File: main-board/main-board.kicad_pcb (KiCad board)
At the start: 2 copper layers, 210 x 130 mm, 173 parts, among them J1 PWR_SELECT, J10 Conn_02x05_Odd_Even, J11 Conn_02x05_Odd_Even, J12 Conn_02x05_Odd_Even, J13 Conn_02x05_Odd_Even, J14 Conn_02x05_Odd_Even, J15 Conn_02x05_Odd_Even, J16 COMM_3, J17 Modular board connector, J18 PWR_EXT_1, J19 PWR_EXT_2, J2 COMM1, J20 COMM_4, J21 COMM_OUT, J3 ICSP, J4 Conn_02x03_Top_Bottom, J5 COMM_2, J7 Conn_02x05_Odd_Even, J8 Conn_02x05_Odd_Even, J9 Conn_02x05_Odd_Even, SW1 RESET, SW10 SW_Push, SW11 SW_Push, SW12 SW_SP3T_x08, SW13 SW_Push, SW14 SW_Push, SW15 SW_Push, SW16 SW_Push, SW17 SW_Push, SW18 SW_Push, SW19 SW_Push, SW2 BTN_LEVEL, SW20 SW_Push, SW21 SW_SP3T_x08, SW22 SW_Push, SW23 SW_Push, SW24 SW_Push, SW25 SW_Push, SW26 SW_Push, SW27 SW_Push, SW28 SW_Push, SW29 SW_Push, SW3 LED_GND, SW30 SW_SP3T_x08, SW31 SW_Push, SW32 SW_Push, SW33 SW_Push, SW34 SW_Push, SW35 SW_Push, SW36 SW_Push, SW37 SW_Push, SW38 SW_Push, SW39 SW_SP3T_x08, SW4 SW_Push, SW41 PWR_EN, SW5 SW_Push, SW6 SW_Push, SW7 SW_Push, SW8 SW_Push, SW9 SW_Push, U1 LM2576HVS-5, U2 AP1117-33, U3 AP1117-18, U4 FT232RL

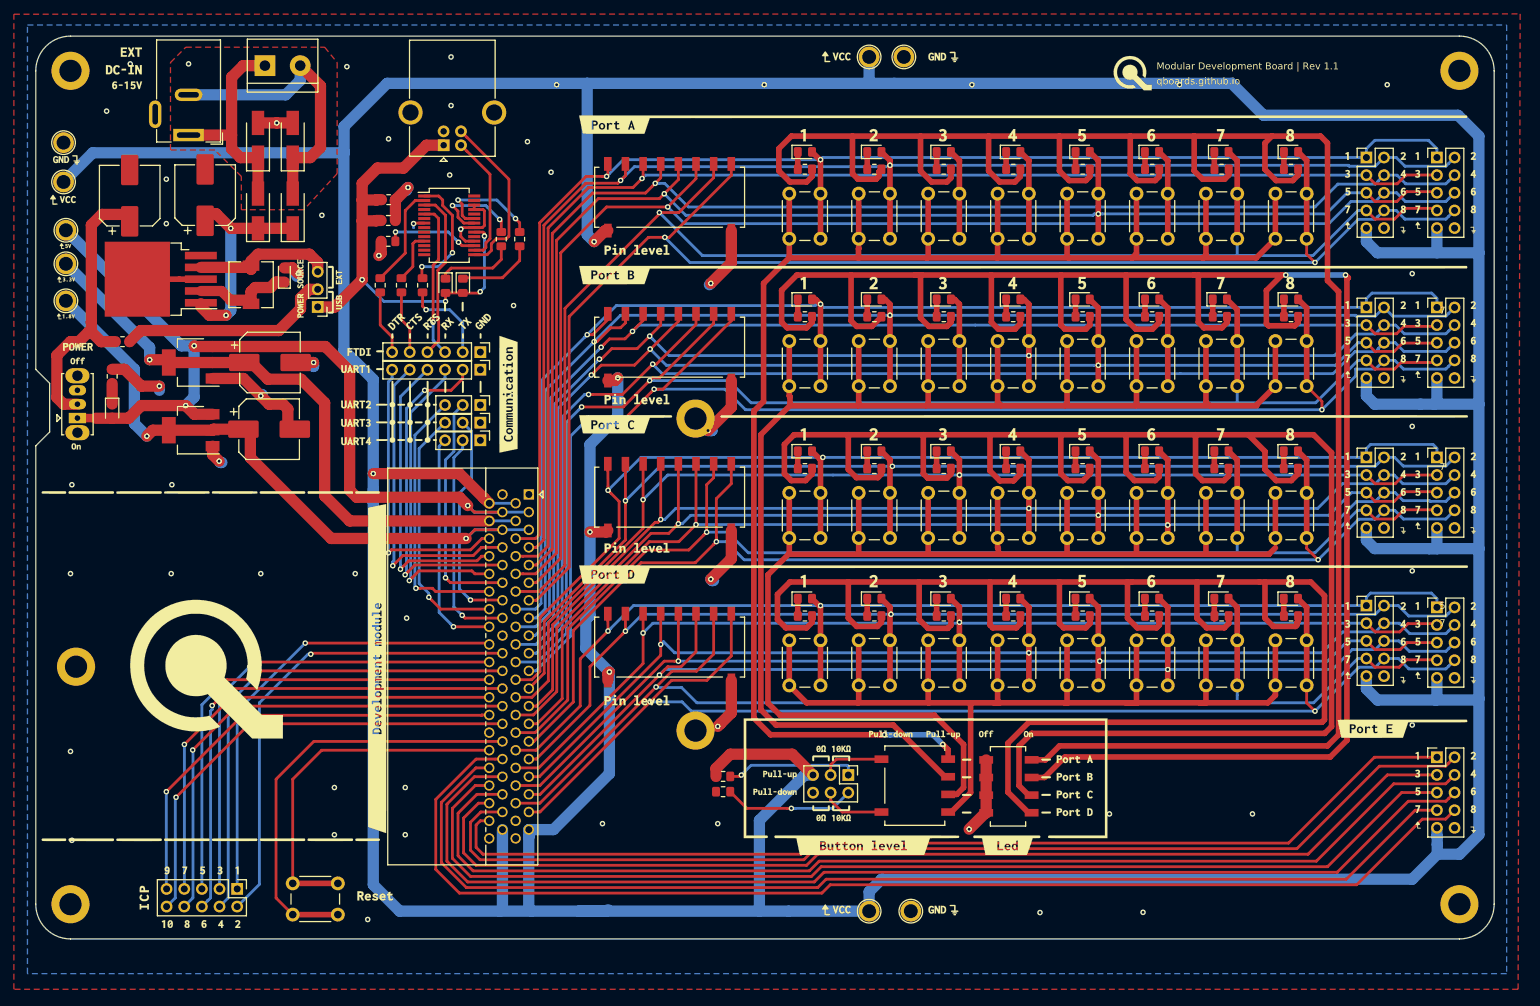
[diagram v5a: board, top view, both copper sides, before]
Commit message: Added pin pullups/downs instead of button level
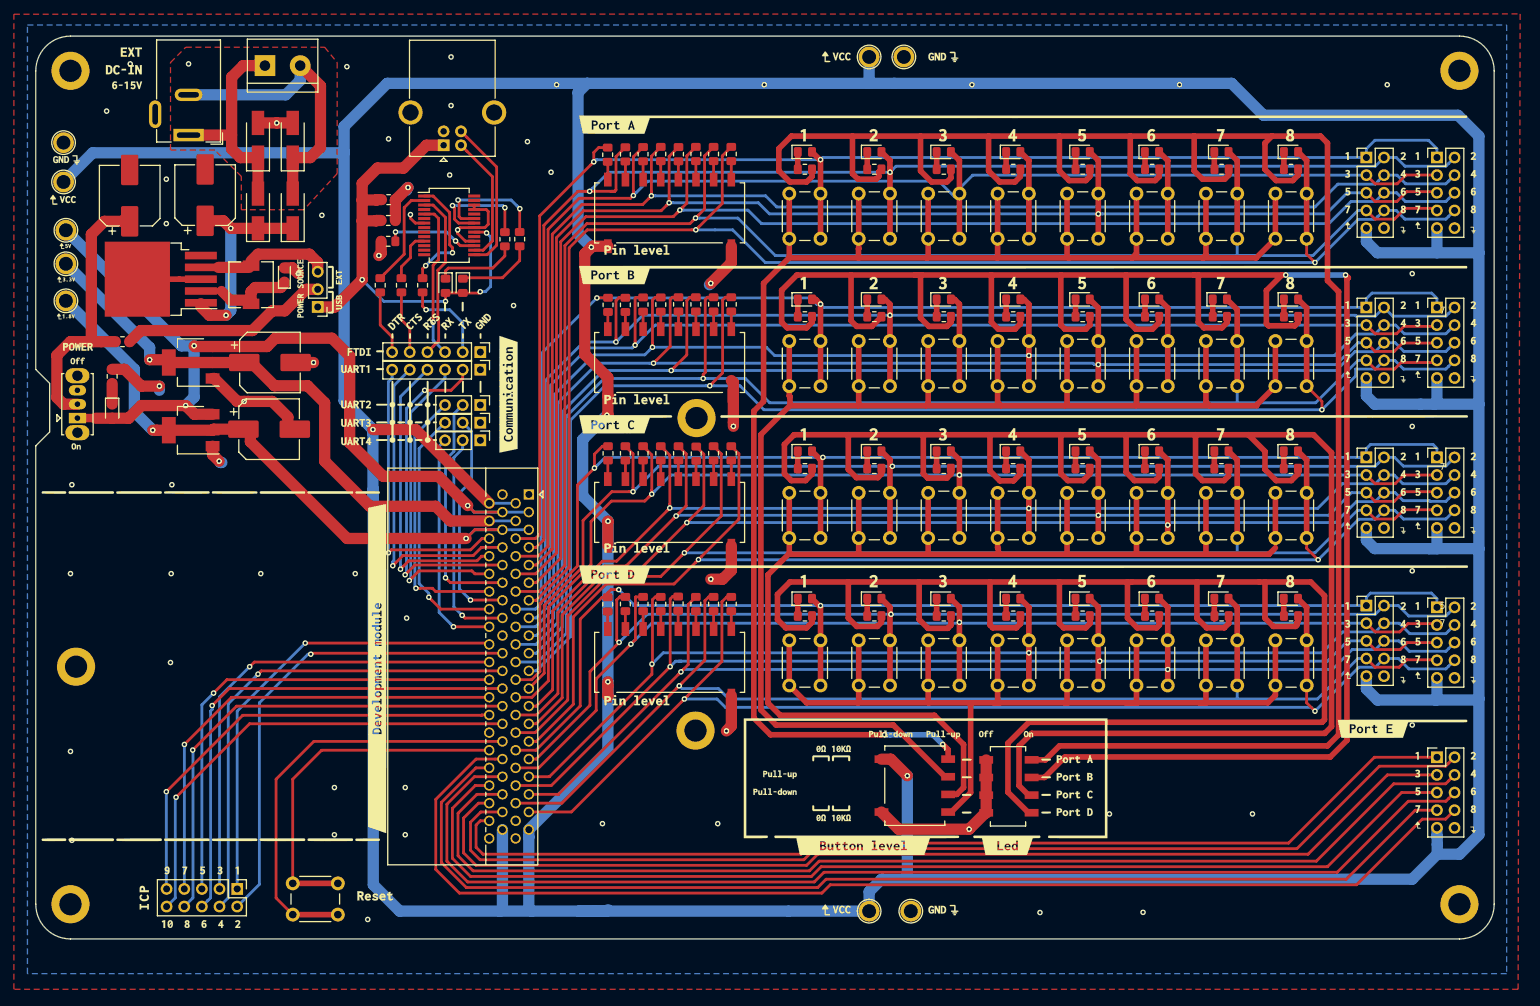
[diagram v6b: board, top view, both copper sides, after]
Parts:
- removed J4: Conn_02x03_Top_Bottom, Connector_PinHeader_2.54mm:PinHeader_2x03_P2.54mm_Vertical
- removed Modular Development Board | Rev 1.1: LOGO_BRD_REF, qboards_aesthetics:logo_url-5mm
- removed R8, R9: R_Small, Resistor_SMD:R_0805_2012Metric_Pad1.15x1.40mm_HandSolder
- removed [BRD_REF]: LOGO_BRD_REF, qboards_aesthetics:logo-20mm
- added R1: 4K7, Resistor_SMD:R_0805_2012Metric_Pad1.15x1.40mm_HandSolder, F.Cu at (119.3, 35.1)
- added R42: 4K7, Resistor_SMD:R_0805_2012Metric_Pad1.15x1.40mm_HandSolder, F.Cu at (121.9, 35.0)
- added R43: 4K7, Resistor_SMD:R_0805_2012Metric_Pad1.15x1.40mm_HandSolder, F.Cu at (124.5, 35.0)
- added R44: 4K7, Resistor_SMD:R_0805_2012Metric_Pad1.15x1.40mm_HandSolder, F.Cu at (127.0, 35.0)
- added R45: 4K7, Resistor_SMD:R_0805_2012Metric_Pad1.15x1.40mm_HandSolder, F.Cu at (129.6, 35.0)
- added R46: 4K7, Resistor_SMD:R_0805_2012Metric_Pad1.15x1.40mm_HandSolder, F.Cu at (132.1, 35.0)
- added R47: 4K7, Resistor_SMD:R_0805_2012Metric_Pad1.15x1.40mm_HandSolder, F.Cu at (134.6, 35.0)
- added R48: 4K7, Resistor_SMD:R_0805_2012Metric_Pad1.15x1.40mm_HandSolder, F.Cu at (137.2, 35.0)
- added R49: 4K7, Resistor_SMD:R_0805_2012Metric_Pad1.15x1.40mm_HandSolder, F.Cu at (119.4, 56.7)
- added R50: 4K7, Resistor_SMD:R_0805_2012Metric_Pad1.15x1.40mm_HandSolder, F.Cu at (121.9, 56.7)
- added R51: 4K7, Resistor_SMD:R_0805_2012Metric_Pad1.15x1.40mm_HandSolder, F.Cu at (124.5, 56.6)
- added R52: 4K7, Resistor_SMD:R_0805_2012Metric_Pad1.15x1.40mm_HandSolder, F.Cu at (127.0, 56.6)
- added R53: 4K7, Resistor_SMD:R_0805_2012Metric_Pad1.15x1.40mm_HandSolder, F.Cu at (129.6, 56.6)
- added R54: 4K7, Resistor_SMD:R_0805_2012Metric_Pad1.15x1.40mm_HandSolder, F.Cu at (132.1, 56.6)
- added R55: 4K7, Resistor_SMD:R_0805_2012Metric_Pad1.15x1.40mm_HandSolder, F.Cu at (134.6, 56.6)
- added R56: 4K7, Resistor_SMD:R_0805_2012Metric_Pad1.15x1.40mm_HandSolder, F.Cu at (137.2, 56.6)
- added R57: 4K7, Resistor_SMD:R_0805_2012Metric_Pad1.15x1.40mm_HandSolder, F.Cu at (119.4, 78.1)
- added R58: 4K7, Resistor_SMD:R_0805_2012Metric_Pad1.15x1.40mm_HandSolder, F.Cu at (121.9, 78.1)
- added R59: 4K7, Resistor_SMD:R_0805_2012Metric_Pad1.15x1.40mm_HandSolder, F.Cu at (124.5, 78.1)
- added R60: 4K7, Resistor_SMD:R_0805_2012Metric_Pad1.15x1.40mm_HandSolder, F.Cu at (127.0, 78.1)
- added R61: 4K7, Resistor_SMD:R_0805_2012Metric_Pad1.15x1.40mm_HandSolder, F.Cu at (129.6, 78.1)
- added R62: 4K7, Resistor_SMD:R_0805_2012Metric_Pad1.15x1.40mm_HandSolder, F.Cu at (132.1, 78.1)
- added R63: 4K7, Resistor_SMD:R_0805_2012Metric_Pad1.15x1.40mm_HandSolder, F.Cu at (134.6, 78.1)
- added R64: 4K7, Resistor_SMD:R_0805_2012Metric_Pad1.15x1.40mm_HandSolder, F.Cu at (137.2, 78.1)
- added R65: 4K7, Resistor_SMD:R_0805_2012Metric_Pad1.15x1.40mm_HandSolder, F.Cu at (119.3, 99.8)
- added R66: 4K7, Resistor_SMD:R_0805_2012Metric_Pad1.15x1.40mm_HandSolder, F.Cu at (121.9, 99.8)
- added R67: 4K7, Resistor_SMD:R_0805_2012Metric_Pad1.15x1.40mm_HandSolder, F.Cu at (124.5, 99.8)
- added R68: 4K7, Resistor_SMD:R_0805_2012Metric_Pad1.15x1.40mm_HandSolder, F.Cu at (127.0, 99.8)
- added R69: 4K7, Resistor_SMD:R_0805_2012Metric_Pad1.15x1.40mm_HandSolder, F.Cu at (129.5, 99.7)
- added R70: 4K7, Resistor_SMD:R_0805_2012Metric_Pad1.15x1.40mm_HandSolder, F.Cu at (132.1, 99.8)
- added R71: 4K7, Resistor_SMD:R_0805_2012Metric_Pad1.15x1.40mm_HandSolder, F.Cu at (134.6, 99.8)
- added R72: 4K7, Resistor_SMD:R_0805_2012Metric_Pad1.15x1.40mm_HandSolder, F.Cu at (137.2, 99.8)
- R3, R4, R5: value 10 -> 10K
- TP_GND3: value VBUS -> GND
- TP_VBUS2: value GND -> VBUS
- moved SW12 2.25 mm to (128.3, 43.5)
- moved SW21 2.20 mm to (128.3, 65.0)
- moved SW39 2.20 mm to (128.3, 108.2)
- moved SW30 2.20 mm to (128.3, 86.6)
- moved R7 0.52 mm to (104.5, 47.2)
- moved H5 0.17 mm to (132.2, 73.0)
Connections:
- SW12 pad 1: /PORT_A_PIN1 -> Net-(R1-Pad2)
- SW12 pad 2: /PORT_A_PIN2 -> Net-(R42-Pad2)
- SW12 pad 3: /PORT_A_PIN3 -> Net-(R43-Pad2)
- SW12 pad 4: /PORT_A_PIN4 -> Net-(R44-Pad2)
- SW12 pad 5: /PORT_A_PIN5 -> Net-(R45-Pad2)
- SW12 pad 6: /PORT_A_PIN6 -> Net-(R46-Pad2)
- SW12 pad 7: /PORT_A_PIN7 -> Net-(R47-Pad2)
- SW12 pad 8: /PORT_A_PIN8 -> Net-(R48-Pad2)
- SW2 pad +: Net-(J4-Pad3) -> VBUS
- SW2 pad -: Net-(J4-Pad4) -> GND
- SW21 pad 1: /PORT_B_PIN1 -> Net-(R49-Pad2)
- SW21 pad 2: /PORT_B_PIN2 -> Net-(R50-Pad2)
- SW21 pad 3: /PORT_B_PIN3 -> Net-(R51-Pad2)
- SW21 pad 4: /PORT_B_PIN4 -> Net-(R52-Pad2)
- SW21 pad 5: /PORT_B_PIN5 -> Net-(R53-Pad2)
- SW21 pad 6: /PORT_B_PIN6 -> Net-(R54-Pad2)
- SW21 pad 7: /PORT_B_PIN7 -> Net-(R55-Pad2)
- SW21 pad 8: /PORT_B_PIN8 -> Net-(R56-Pad2)
- SW30 pad 1: /PORT_C_PIN1 -> Net-(R57-Pad2)
- SW30 pad 2: /PORT_C_PIN2 -> Net-(R58-Pad2)
- SW30 pad 3: /PORT_C_PIN3 -> Net-(R59-Pad2)
- SW30 pad 4: /PORT_C_PIN4 -> Net-(R60-Pad2)
- SW30 pad 5: /PORT_C_PIN5 -> Net-(R61-Pad2)
- SW30 pad 6: /PORT_C_PIN6 -> Net-(R62-Pad2)
- SW30 pad 7: /PORT_C_PIN7 -> Net-(R63-Pad2)
- SW30 pad 8: /PORT_C_PIN8 -> Net-(R64-Pad2)
- SW39 pad 1: /PORT_D_PIN1 -> Net-(R65-Pad2)
- SW39 pad 2: /PORT_D_PIN2 -> Net-(R66-Pad2)
- SW39 pad 3: /PORT_D_PIN3 -> Net-(R67-Pad2)
- SW39 pad 4: /PORT_D_PIN4 -> Net-(R68-Pad2)
- SW39 pad 5: /PORT_D_PIN5 -> Net-(R69-Pad2)
- SW39 pad 6: /PORT_D_PIN6 -> Net-(R70-Pad2)
- SW39 pad 7: /PORT_D_PIN7 -> Net-(R71-Pad2)
- SW39 pad 8: /PORT_D_PIN8 -> Net-(R72-Pad2)
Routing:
- net Net-(J4-Pad1): track 19.0 -> 0.00 mm, vias 1 -> 0
- net Net-(J4-Pad2): track 18.9 -> 0.00 mm, vias 1 -> 0
- net Net-(J4-Pad3): track 9.23 -> 0.00 mm
- net Net-(J4-Pad4): track 9.23 -> 0.00 mm
- net /PORT_A_PIN2: track 199.9 -> 208.3 mm
- net /PORT_C_PIN7: track 180.9 -> 187.3 mm
- net /PORT_C_PIN8: track 185.3 -> 191.6 mm
- net /PORT_B_PIN3: track 188.3 -> 194.2 mm, vias 2 -> 1
- net /PORT_A_PIN8: track 213.6 -> 219.4 mm
- net /PORT_D_PIN2: track 162.4 -> 167.9 mm
- net /PORT_D_PIN3: track 160.7 -> 166.2 mm
- net GND: track 115.9 -> 120.9 mm
- net /PORT_D_PIN4: track 163.3 -> 168.1 mm
- net /PORT_C_PIN3: track 175.0 -> 179.8 mm
- net /PORT_C_PIN6: track 175.8 -> 180.5 mm
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
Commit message: Fixed some routing
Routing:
- net Net-(J17-Pad20): track 44.8 -> 42.7 mm
- net GND: track 120.9 -> 119.0 mm
- net /PORT_B_PIN6: track 198.2 -> 196.6 mm, vias 1 -> 2
- net Net-(J17-Pad24): track 39.7 -> 38.1 mm
- net +3V3: track 86.0 -> 87.6 mm
- net +5V: track 127.0 -> 128.5 mm
- net /PORT_C_PIN1: track 180.4 -> 181.6 mm
- net Net-(J17-Pad14): track 46.1 -> 44.9 mm
- net Net-(J16-Pad3): track 36.7 -> 35.5 mm
- net +1V8: track 91.9 -> 91.1 mm
- net VBUS: track 893.7 -> 893.0 mm

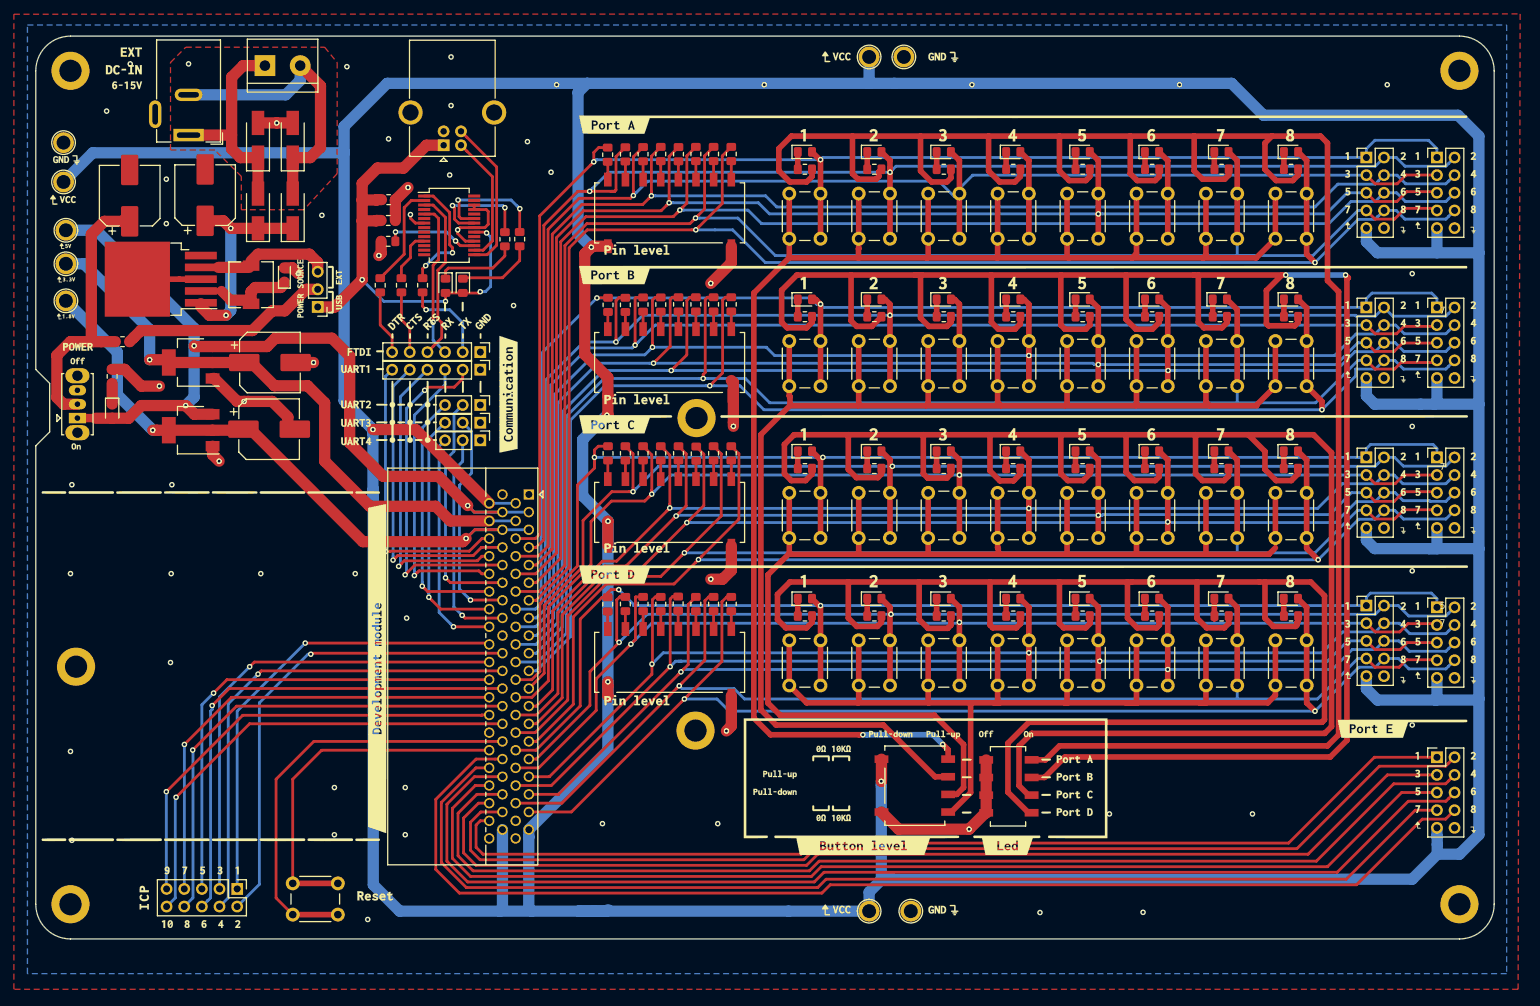
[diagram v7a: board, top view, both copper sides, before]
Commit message: Added probe cutouts
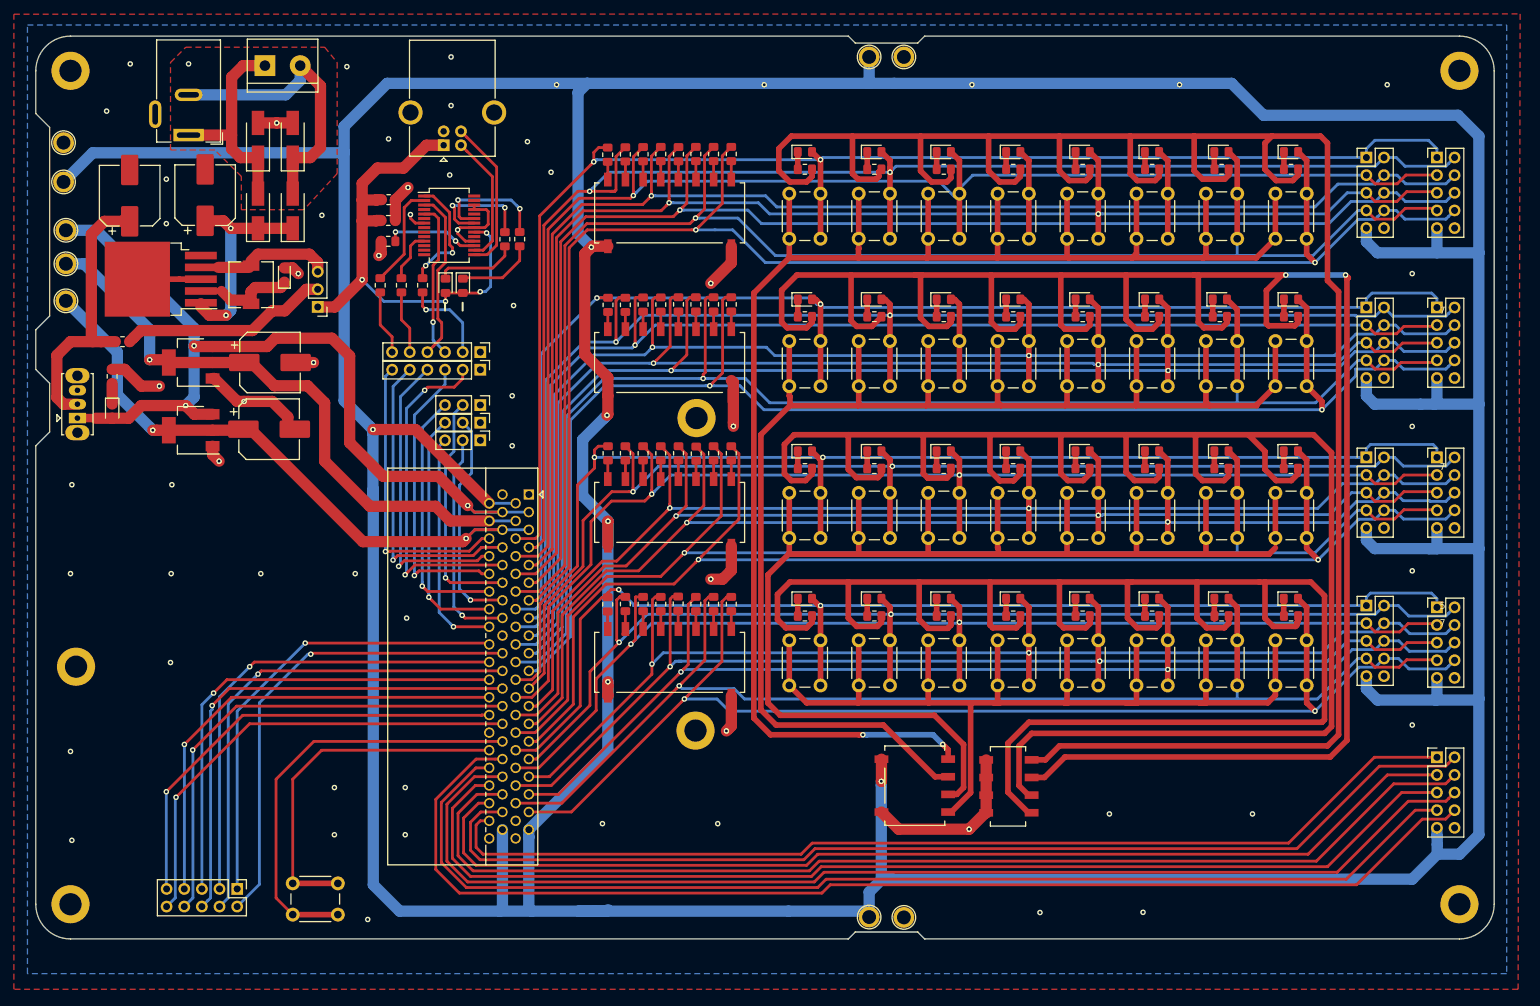
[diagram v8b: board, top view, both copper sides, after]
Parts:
- removed ?: , 
- TP_GND3: value GND -> VBUS
- TP_VBUS2: value VBUS -> GND
- moved TP_GND2 1.35 mm to (162.0, 144.9)
- moved TP_VBUS1 0.85 mm to (157.0, 144.8)
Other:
- outline, holes or cut-outs redrawn
